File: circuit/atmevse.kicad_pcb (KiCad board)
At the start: 2 copper layers, 86.5 x 103 mm, 94 parts, among them J1 Screw_Terminal_01x10, J2 Screw_Terminal_01x18, J3 Conn_01x04, J4 Conn_02x04_Top_Bottom, J5 Conn_02x04_Top_Bottom, Q1 BSS138, U1 AQH3223, U10 ATmega4808-X, U11 LM7332, U12 CPC1114N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

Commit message: Update first layout draft
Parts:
- J3, RV1, RV2, RV3: moved to B.Cu
- R13: footprint Resistor_SMD:R_0805_2012Metric_Pad1.15x1.40mm_HandSolder -> Resistor_SMD:R_0603_1608Metric_Pad1.05x0.95mm_HandSolder
- moved C16 164.8 mm to (171.9, 132.4), turned to 270 degrees
- moved C21 163.9 mm to (171.9, 128.4), turned to 90 degrees
- moved J3 163.5 mm to (187.7, 144.2), turned to 90 degrees
- moved C17 156.2 mm to (148.2, 103.2), turned to 90 degrees
- moved R6 148.6 mm to (145.6, 93.6)
- moved R5 148.4 mm to (145.6, 90.6)
- moved J4 140.4 mm to (126.8, 136.0), turned to 180 degrees
- moved J5 134.0 mm to (137.5, 136.0), turned to 180 degrees
- moved R9 133.8 mm to (148.8, 81.0), turned to 90 degrees
- moved R27 129.6 mm to (179.6, 126.7)
- moved R10 129.5 mm to (150.6, 81.0), turned to 90 degrees
- moved R26 128.7 mm to (175.8, 126.7)
- moved R3 128.6 mm to (149.1, 90.6)
- moved RV3 124.9 mm to (124.5, 113.3), turned to 0 degrees
- moved U9 124.4 mm to (157.4, 125.4), turned to 180 degrees
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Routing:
- net +12V: track 0.00 -> 103.7 mm
- net /Mains and Power Circuitry/N: track 0.00 -> 99.4 mm
- net +3V3: track 0.00 -> 92.2 mm, vias 0 -> 6
- net /ATmega4808 and Peripherals/ESP_IO12: track 0.00 -> 68.5 mm
- net /Mains and Power Circuitry/C_L3: track 0.00 -> 62.6 mm, vias 0 -> 2
- net Net-(F2-Pad1): track 0.00 -> 61.1 mm
- net /Mains and Power Circuitry/C_L1: track 0.00 -> 56.3 mm
- net /ATmega4808 and Peripherals/EN: track 0.00 -> 54.5 mm, vias 0 -> 2
- net /ATmega4808 and Peripherals/ATmega_RX0: track 0.00 -> 52.3 mm, vias 0 -> 4
- net /ATmega4808 and Peripherals/ATmega_RESET: track 0.00 -> 51.6 mm, vias 0 -> 2
- net /Mains and Power Circuitry/C_L2: track 0.00 -> 49.6 mm, vias 0 -> 2
- net /ATmega4808 and Peripherals/ATmega_TX0: track 0.00 -> 48.5 mm, vias 0 -> 2
- net /Analog Section and Low Voltage Outputs/BIAS: track 0.00 -> 44.8 mm, vias 0 -> 2
- net /ATmega4808 and Peripherals/ESP_RX2: track 0.00 -> 43.0 mm
- net /ATmega4808 and Peripherals/ATmega_UDPI: track 0.00 -> 38.5 mm, vias 0 -> 4
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
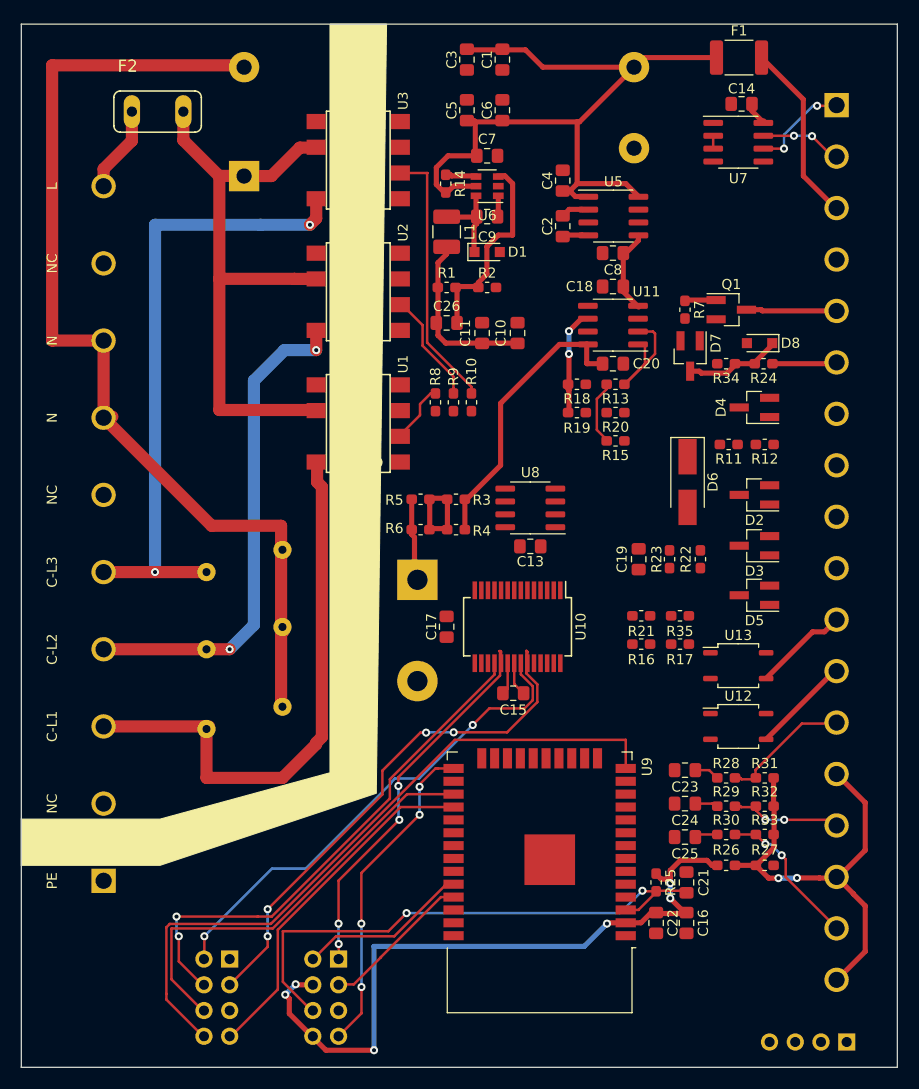
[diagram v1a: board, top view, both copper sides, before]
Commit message: Finish Rev1 PCB Layout and send off to fab
PCB layout is done now, collect Revisions in REVISION.md
TODO updated with current tasks
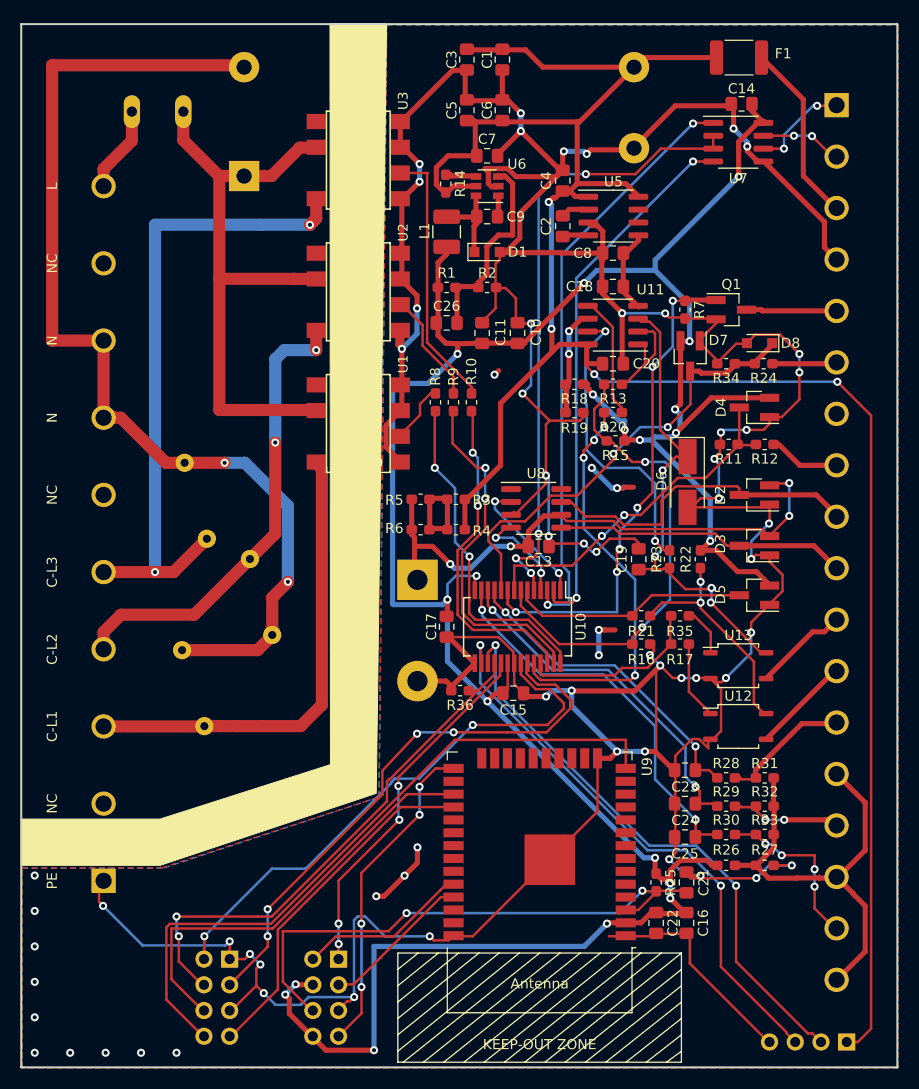
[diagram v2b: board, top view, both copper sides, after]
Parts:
- added R36: Reset Pulldown, Resistor_SMD:R_0603_1608Metric_Pad1.05x0.95mm_HandSolder, F.Cu at (149.5, 109.5)
- F2: moved to B.Cu
- moved RV2 9.89 mm to (128.8, 96.5), turned to 270 degrees
- moved RV1 3.29 mm to (124.5, 94.5), turned to 90 degrees
- moved C13 0.82 mm to (157.2, 95.2)
- moved U8 0.57 mm to (157.0, 91.5), turned to 0 degrees
- moved RV3 0.35 mm to (124.2, 113.0), turned to 90 degrees
- moved R13 0.25 mm to (164.6, 79.2)
- moved R18 0.25 mm to (160.8, 79.2)
- moved R19 0.25 mm to (160.8, 82.0)
- moved R20 0.25 mm to (164.6, 82.0)
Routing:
- net GND: track 3.34 -> 539.6 mm, vias 0 -> 65
- net +3V3: track 92.2 -> 275.9 mm, vias 6 -> 20
- net +12V: track 103.7 -> 214.3 mm, vias 0 -> 4
- net /ATmega4808 and Peripherals/RS485_XDIR: track 1.31 -> 62.0 mm, vias 0 -> 4
- net /ATmega4808 and Peripherals/RS485_RX: track 0.00 -> 59.0 mm, vias 0 -> 2
- net /ATmega4808 and Peripherals/ATmega_RX2: track 0.00 -> 57.5 mm, vias 0 -> 2
- net /ATmega4808 and Peripherals/ATmega_TX2: track 0.00 -> 56.0 mm, vias 0 -> 2
- net /ATmega4808 and Peripherals/RS485_TX: track 0.00 -> 53.5 mm, vias 0 -> 2
- net Net-(C12-Pad1): track 8.17 -> 57.1 mm, vias 0 -> 4
- net /Analog Section and Low Voltage Outputs/CP_to_relay: track 0.00 -> 47.0 mm, vias 0 -> 4
- net Net-(Q1-Pad1): track 3.30 -> 50.1 mm, vias 0 -> 6
- net /ATmega4808 and Peripherals/CP: track 6.32 -> 47.5 mm, vias 0 -> 2
- net /ATmega4808 and Peripherals/PWM_Out: track 0.00 -> 40.7 mm, vias 0 -> 4
- net /ATmega4808 and Peripherals/CT2: track 2.27 -> 39.1 mm, vias 0 -> 2
- net /ATmega4808 and Peripherals/Button: track 9.52 -> 44.4 mm, vias 0 -> 2
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- added copper zone on B.Cu, net GND
- added copper zone on F.Cu, net GND
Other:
- rule solder_mask_min_width: 0.25 -> 0.09
- board text added: "ATmevse Rev1.0 06/2020"

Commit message: Finish Revision 1.1 layout
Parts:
- removed R36: Reset Pulldown, Resistor_SMD:R_0603_1608Metric_Pad1.05x0.95mm_HandSolder
- added D10: BAT54S, Package_TO_SOT_SMD:SOT-23_Handsoldering, F.Cu at (177.7, 133.4)
- added D11: BAT54S, Package_TO_SOT_SMD:SOT-23_Handsoldering, F.Cu at (164.7, 89.2)
- added D9: BAT54S, Package_TO_SOT_SMD:SOT-23_Handsoldering, F.Cu at (177.7, 138.3)
- added J6: Screw_Terminal_01x09, atmevse-footprints:lv_screw_9pin_1, B.Cu at (187.1, 49.8)
- added J7: Screw_Terminal_01x09, atmevse-footprints:lv_screw_9pin_2, B.Cu at (186.9, 99.5)
- added R37: 1k, Resistor_SMD:R_0603_1608Metric_Pad1.05x0.95mm_HandSolder, F.Cu at (124.8, 142.0)
- added R38: 1k, Resistor_SMD:R_0603_1608Metric_Pad1.05x0.95mm_HandSolder, F.Cu at (124.8, 144.5)
- C16: footprint Capacitor_SMD:C_0805_2012Metric_Pad1.15x1.40mm_HandSolder -> Capacitor_Tantalum_SMD:CP_EIA-2012-15_AVX-P_Pad1.30x1.05mm_HandSolder
- D8: value 3.3V Zener -> BAT54S; footprint Diode_SMD:D_SOD-323_HandSoldering -> Package_TO_SOT_SMD:SOT-23_Handsoldering
- J1: value Screw_Terminal_01x10 -> Screw_Terminal_01x05; footprint atmevse-footprints:CUI_TB005-762-10GR -> atmevse-footprints:hv_screw_5pin_1
- J2: value Screw_Terminal_01x18 -> Screw_Terminal_01x05; footprint atmevse-footprints:CUI_TB004-508-18BE -> atmevse-footprints:hv_screw_5pin_2
- J3: footprint Connector_PinHeader_2.54mm:PinHeader_1x04_P2.54mm_Vertical -> atmevse-footprints:UART2-Header
- J4: value Conn_02x04_Top_Bottom -> Conn_01x04; footprint Connector_PinHeader_2.54mm:PinHeader_2x04_P2.54mm_Vertical -> atmevse-footprints:UART0-Header
- J5: footprint Connector_PinHeader_2.54mm:PinHeader_2x04_P2.54mm_Vertical -> atmevse-footprints:PROGRAM-Header
- R24: value 100 -> 1k
- R34: value 33 -> 1k
- U4: value MPM-05-12 -> IRM-10-12
- U9: moved to B.Cu
- moved J2 81.7 mm to (114.2, 89.5), turned to 90 degrees
- moved R34 80.3 mm to (124.9, 139.4), turned to 0 degrees
- moved J3 78.9 mm to (109.0, 137.9), turned to 270 degrees
- moved D8 67.6 mm to (177.6, 142.8), turned to 0 degrees
- moved RV1 17.0 mm to (126.6, 77.6), turned to 270 degrees
- moved RV3 6.47 mm to (128.8, 117.6)
- moved J5 4.81 mm to (137.2, 131.2)
- moved F2 4.32 mm to (119.6, 48.0)
- moved RV2 3.37 mm to (126.6, 93.9)
- moved J1 3.33 mm to (114.4, 131.6)
- moved R6 3.09 mm to (144.1, 90.9), turned to 90 degrees
- moved R4 2.99 mm to (147.8, 90.9), turned to 90 degrees
- moved J4 2.24 mm to (128.8, 136.9)
- moved R3 0.59 mm to (149.6, 90.9), turned to 90 degrees
- moved R5 0.43 mm to (145.9, 90.9), turned to 90 degrees
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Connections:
- net /ATmega4808 and Peripherals/ATmega_UDPI renamed Net-(J5-Pad1)
- D8 pad 1: /ATmega4808 and Peripherals/Button -> GND
- D8 pad 2: GND -> +3V3
- J1 pad 2: Net-(J1-Pad2) -> /Mains and Power Circuitry/N
- J1 pad 4: /Mains and Power Circuitry/C_L2 -> /Mains and Power Circuitry/N
- J1 pad 5: /Mains and Power Circuitry/C_L3 -> /Mains and Power Circuitry/C_L2
- J2 pad 1: /ATmega4808 and Peripherals/RS485_A -> /Mains and Power Circuitry/N
- J2 pad 2: /ATmega4808 and Peripherals/RS485_B -> /Mains and Power Circuitry/C_L3
- J2 pad 3: /Analog Section and Low Voltage Outputs/12V_Fused -> /Mains and Power Circuitry/N
- J2 pad 4: GND -> Net-(J2-Pad4)
- J2 pad 5: /ATmega4808 and Peripherals/LED -> /Mains and Power Circuitry/L
- J5 pad 2: /ATmega4808 and Peripherals/ESP_RX0 -> /ATmega4808 and Peripherals/ESP_TX0
- J5 pad 3: /ATmega4808 and Peripherals/ESP_TX0 -> /ATmega4808 and Peripherals/ESP_RX0
- J5 pad 4: +3V3 -> /ATmega4808 and Peripherals/IO0
- J5 pad 6: /ATmega4808 and Peripherals/EN -> +3V3
- J5 pad 7: /ATmega4808 and Peripherals/IO0 -> /ATmega4808 and Peripherals/ESP_IO15
- J5 pad 8: +3V3 -> /ATmega4808 and Peripherals/EN
- R24 pad 1: Net-(J2-Pad6) -> Net-(J6-Pad5)
- R3 pad 1: Net-(R3-Pad1) -> Net-(C12-Pad1)
- R34 pad 1: /ATmega4808 and Peripherals/Button -> /ATmega4808 and Peripherals/ESP_RX2
- R34 pad 2: GND -> /ATmega4808 and Peripherals/ATmega_TX0
- R4 pad 1: Net-(R3-Pad1) -> Net-(C12-Pad1)
- R5 pad 2: Net-(R3-Pad1) -> +12V
- R6 pad 2: Net-(R3-Pad1) -> +12V
- U4 pad 1: Net-(F2-Pad1) -> /Mains and Power Circuitry/N
- U4 pad 2: /Mains and Power Circuitry/N -> Net-(F2-Pad1)
- U4 pad 3: +12V -> GND
- U4 pad 4: GND -> +12V
- U9 pad 23: Net-(U9-Pad23) -> /ATmega4808 and Peripherals/ESP_IO15
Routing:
- net /Mains and Power Circuitry/N: track 104.1 -> 153.7 mm
- net /ATmega4808 and Peripherals/ESP_IO15: track 0.00 -> 40.5 mm, vias 0 -> 3
- net GND: track 539.6 -> 578.8 mm, vias 65 -> 52
- net /ATmega4808 and Peripherals/CT0: track 31.8 -> 63.9 mm, vias 2 -> 4
- net +3V3: track 275.9 -> 302.7 mm
- net /Mains and Power Circuitry/C_L3: track 64.0 -> 39.0 mm, vias 2 -> 1
- net /ATmega4808 and Peripherals/ESP_RX0: track 18.0 -> 41.8 mm, vias 0 -> 5
- net /ATmega4808 and Peripherals/CT1: track 35.4 -> 58.3 mm, vias 2 -> 4
- net /Analog Section and Low Voltage Outputs/12V_Fused: track 18.1 -> 39.2 mm
- net /ATmega4808 and Peripherals/ESP_TX2: track 35.0 -> 55.1 mm, vias 0 -> 3
- net /ATmega4808 and Peripherals/ESP_TX0: track 14.9 -> 35.0 mm, vias 0 -> 4
- net /ATmega4808 and Peripherals/ESP_IO12: track 68.5 -> 49.0 mm, vias 0 -> 1
- net /ATmega4808 and Peripherals/IO0: track 32.3 -> 51.0 mm, vias 4 -> 1
- net +12V: track 214.3 -> 197.7 mm, vias 4 -> 3
- net /ATmega4808 and Peripherals/ESP_RX2: track 43.0 -> 56.7 mm, vias 0 -> 3
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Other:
- board text added: "FGCCS-Ctrl22 Rev1.1 08/2020"
- board text removed: "ATmevse Rev1.0 06/2020"
